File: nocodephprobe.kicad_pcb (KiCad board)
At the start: 2 copper layers, 76 x 80.9 mm, 37 parts, among them J1 BNC (pH Probe), J2 10K, Q1 2N7002, SW1 SW_SPST, U1 TLV272, U2 ICL7106CPL, U3 MCP1501T-10E/CHY, U4 VI-302-DP-RC-S

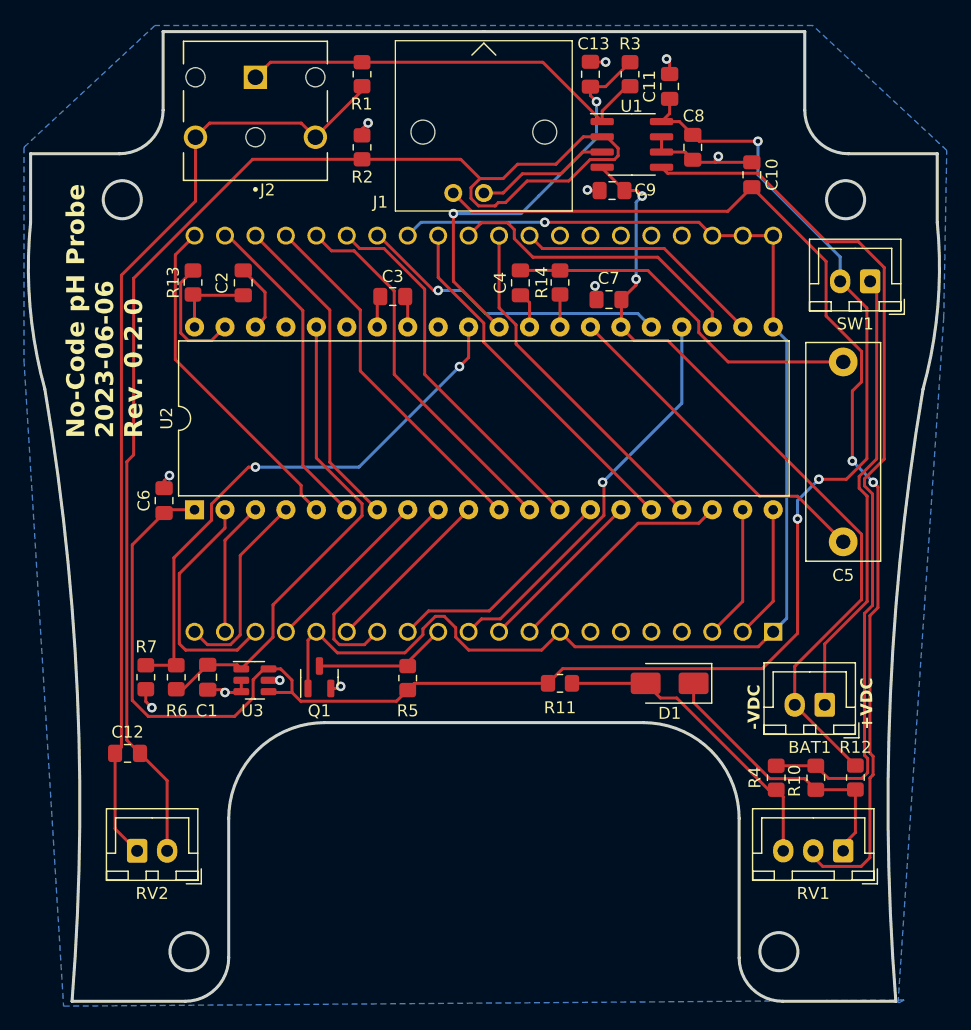
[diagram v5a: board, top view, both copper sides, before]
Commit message: Implement [optional] input protection
D2 will clamp the input to 3 diode drops from either rail (~1.8V). This
keeps the input within the safe range for the TLV272. R15 limits the
current in case of overvoltage. The diodes in D3 and D4 set a bias point
two diode drops below the positive rail and above the negative rail to
minimize the reverse voltage (and therefore leakage current) across the
D2 diodes.

Since the D2 diodes are reverse-biased normally, they should not affect
normal input. However, the tricky part is finding diodes with low enough
(preferabley <10pA) reverse leakage current. These BAV199 diodes are by
far the most cost effective solution I found ($0.18 in single quantities
of dual diodes); they have a typical
leakage current of only 3pA @75V (so probably much less at ~2V) -- but
they are only guaranteed to be less than 5nA which is way too high. So
technically they should be characterized before using them in circuit.

Other potential solutions:
- diode-connected JFET like the MMBF4117 with max 10pA Igss
  (https://www.digikey.com/en/products/detail/onsemi/MMBF4117/1049290).
  But these are $1-$5 each.
- diode-connect BJTs like the 2N3904 are supposed to be very low
  leakage. These are cheap, but I'd have to experiment with them.

I think it is generally safe to leave off the protection diodes all
together (but might as well leave R15; it barely contributes to input
impedance). But if you do, I'd recommend connecting the probe to the
meter before powerint it on just to make sure the input of the op-amp
does not float above its rails. The TLV272 and other op-amps with low
current bias seem to have no or minimal static protection.
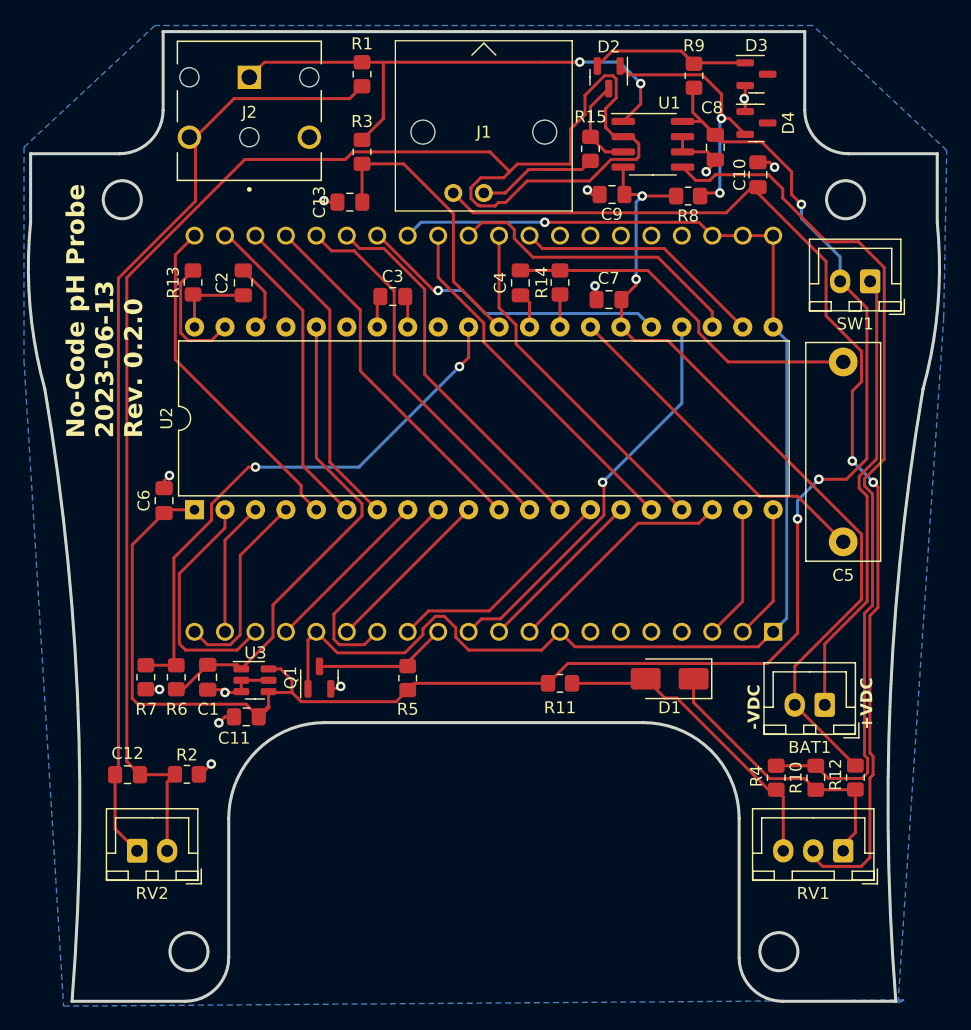
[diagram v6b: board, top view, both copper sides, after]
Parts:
- added D2: BAV199, Package_TO_SOT_SMD:SOT-23, F.Cu at (159.0, 57.1)
- added D3: BAV199, Package_TO_SOT_SMD:SOT-23, F.Cu at (171.3, 56.9)
- added D4: BAV199, Package_TO_SOT_SMD:SOT-23, F.Cu at (171.3, 61.0)
- added R15: 1k, Resistor_SMD:R_0805_2012Metric_Pad1.20x1.40mm_HandSolder, F.Cu at (157.5, 63.1)
- added R8: 5k, Resistor_SMD:R_0805_2012Metric_Pad1.20x1.40mm_HandSolder, F.Cu at (165.6, 67.1)
- added R9: 5k, Resistor_SMD:R_0805_2012Metric_Pad1.20x1.40mm_HandSolder, F.Cu at (166.1, 57.0)
- moved C11 63.3 mm to (128.8, 110.5), turned to 180 degrees
- moved R2 54.3 mm to (123.8, 115.3), turned to 180 degrees
- moved R3 23.3 mm to (138.4, 63.4), turned to -90 degrees
- moved C13 22.7 mm to (137.4, 67.6), turned to 0 degrees
- moved C8 1.88 mm to (167.9, 63.0)
- moved C12 1.78 mm to (118.9, 115.3)
- moved U1 1.75 mm to (162.7, 62.7)
- moved C10 0.51 mm to (171.4, 65.3)
- moved J2 0.51 mm to (129.0, 57.1)
- moved D1 0.38 mm to (164.1, 107.3)
- moved C9 0.33 mm to (159.3, 66.9)
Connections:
- J2 pad 2: Net-(C12-Pad2) -> (no net)
- U1 pad 3: Net-(J1-In) -> /input
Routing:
- net Net-(D2-A): track 0.00 -> 22.0 mm, vias 0 -> 2
- net Net-(U1A--): track 113.3 -> 132.2 mm
- net Net-(D2-K): track 0.00 -> 12.5 mm
- net Net-(U2-IN_LO): track 34.2 -> 23.6 mm, vias 2 -> 0
- net /scaled: track 35.5 -> 44.9 mm, vias 0 -> 2
- net /input: track 0.00 -> 7.91 mm
- net -VDC: track 67.0 -> 69.3 mm
- net Net-(J1-In): track 11.3 -> 10.0 mm
- net Net-(U1B-+): track 73.8 -> 72.9 mm
- net GND: track 24.6 -> 25.2 mm, vias 11 -> 12

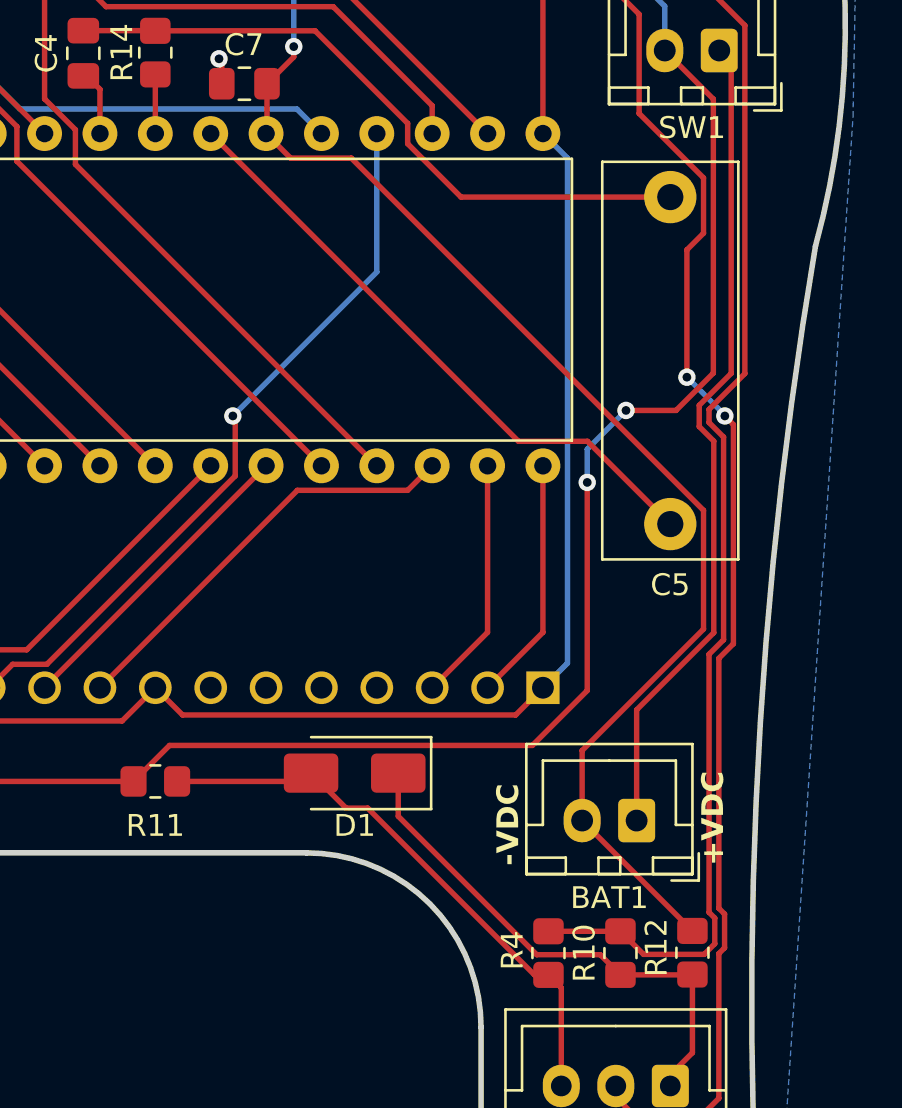
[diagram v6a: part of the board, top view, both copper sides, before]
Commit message: Specify cheaper Schottky diodes
Also add one as reverse-voltage protection to protect op-amp input (D5)
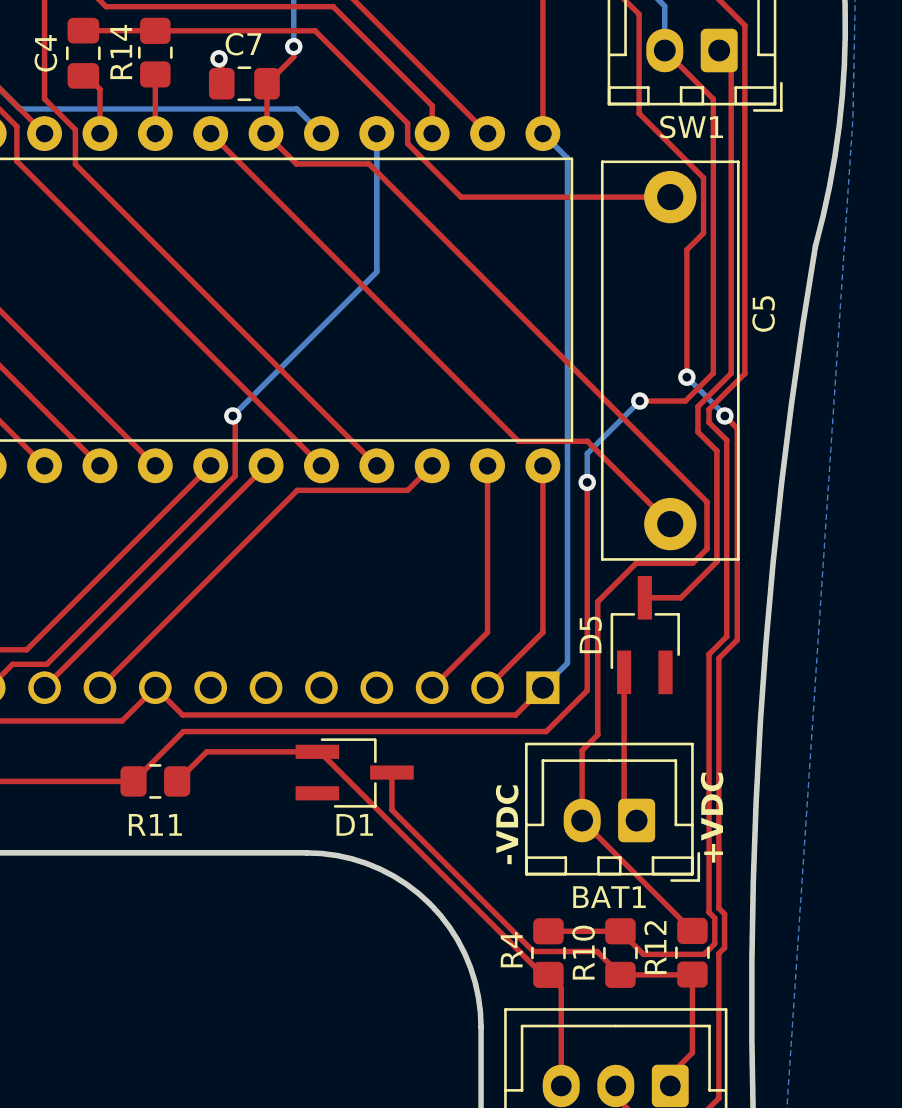
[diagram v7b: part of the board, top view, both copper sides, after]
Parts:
- added D5: BAT54-Q, Package_TO_SOT_SMD:TSOT-23_HandSoldering, F.Cu at (177.4, 101.0)
- D1: value SS14 -> BAT54-Q; footprint Diode_SMD:D_SMA -> Package_TO_SOT_SMD:TSOT-23_HandSoldering
- R8, R9: value 5k -> 4.7k
- turned D1 to 0 degrees
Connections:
- D1 pad 1: Net-(D1-K) -> Net-(D1-A)
- D1 pad 2: Net-(D1-A) -> (no net)
- SW1 pad 1: Net-(BAT1-+) -> Net-(D5-K)
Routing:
- net Net-(BAT1-+): track 37.9 -> 7.04 mm
- net Net-(D5-K): track 0.00 -> 28.7 mm
- net -VDC: track 69.3 -> 71.2 mm
- net Net-(D1-A): track 25.9 -> 26.7 mm

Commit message: Use SPDT for power switch
I decided on these MTS-103 mini toggle switches, to be mounted next to BNC
(and connected with wires to JST XH connector):

https://www.amazon.com/dp/B07CJFVZ7M
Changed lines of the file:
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@@
     (property "Sheetfile" "nocodephprobe.kicad_sch")
     (property "Sheetname" "")
-    (property "ki_description" "Single Pole Single Throw (SPST) switch")
-    (property "ki_keywords" "switch lever")
+    (property "ki_description" "Switch, single pole double throw")
+    (property "ki_keywords" "switch single-pole double-throw spdt ON-ON")
     (attr through_hole)
     (fp_text reference "SW1" (at 1.25 -3.55 180) (layer "F.SilkS")
@@
       (stroke (width 0.1) (type solid)) (layer "F.Fab"))
     (pad "1" thru_hole roundrect (at 0 0 180) (size 1.7 2) (drill 1) (layers "*.Cu" "*.Mask") (roundrect_rratio 0.147059)
-      (net 65 "Net-(D5-K)") (pinfunction "A") (pintype "passive"))
+      (net 65 "Net-(D5-K)") (pinfunction "B") (pintype "passive"))
     (pad "2" thru_hole oval (at 2.5 0 180) (size 1.7 2) (drill 1) (layers "*.Cu" "*.Mask")
-      (net 1 "+VDC") (pinfunction "B") (pintype "passive"))
+      (net 1 "+VDC") (pinfunction "C") (pintype "passive"))
     (model "${KICAD6_3DMODEL_DIR}/Connector_JST.3dshapes/JST_XH_B2B-XH-A_1x02_P2.50mm_Vertical.wrl"
       (offset (xyz 0 0 0))
@@
   (segment (start 180.7008 97.6188) (end 179.0474 99.2722) (width 0.254) (layer "F.Cu") (net 65))
   (segment (start 180.7008 92.5374) (end 180.7008 97.6188) (width 0.254) (layer "F.Cu") (net 65))
-  (segment (start 181.356 74.716) (end 180.808 74.168) (width 0.25) (layer "F.Cu") (net 65))
   (segment (start 180.249601 92.086201) (end 179.832 91.6686) (width 0.25) (layer "F.Cu") (net 65))
   (segment (start 179.832 90.502799) (end 181.356 88.978799) (width 0.25) (layer "F.Cu") (net 65))
+  (segment (start 180.808 74.168) (end 181.356 74.716) (width 0.25) (layer "F.Cu") (net 65))
   (segment (start 180.249601 92.086201) (end 180.7008 92.5374) (width 0.254) (layer "F.Cu") (net 65))
-  (segment (start 181.356 88.978799) (end 181.356 74.716) (width 0.25) (layer "F.Cu") (net 65))
+  (segment (start 181.356 74.716) (end 181.356 88.978799) (width 0.25) (layer "F.Cu") (net 65))
   (zone (net 4) (net_name "GND") (layer "B.Cu") (hatch edge 0.5)
     (connect_pads (clearance 0.5))
